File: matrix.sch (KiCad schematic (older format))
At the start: 130 parts, among them SW1 Esc, SW10 9, SW11 0, SW12 -, SW13 =, SW14 Back, SW15 Ins, SW16 Tab, SW17 Q, SW18 W, SW19 E, SW2 1, SW20 R, SW21 T, SW22 Y, SW23 U, SW24 I, SW25 O, SW26 P, SW27 [ {, SW28 ] }, SW29 | \\, SW3 2, SW30 Del, SW31 Caps Lock, SW32 A, SW33 S, SW34 D, SW35 F, SW36 G, SW37 H, SW38 J, SW39 K, SW4 3, SW40 L, SW41 ; :, SW42 ' @, SW43 Enter, SW44 L Shifth, SW45 Z, SW46 X, SW47 C, SW48 V, SW49 B, SW5 4, SW50 N, SW51 M, SW52 , <, SW53 . >, SW54 / ?, SW55 R Shift, SW56 Up, SW57 L Ctrl, SW58 Home, SW59 L Alt, SW6 5, SW60 Space, SW61 R Alt, SW62 Fn, SW63 Left, SW64 Down, SW65 Right, SW7 6, SW8 7, SW9 8

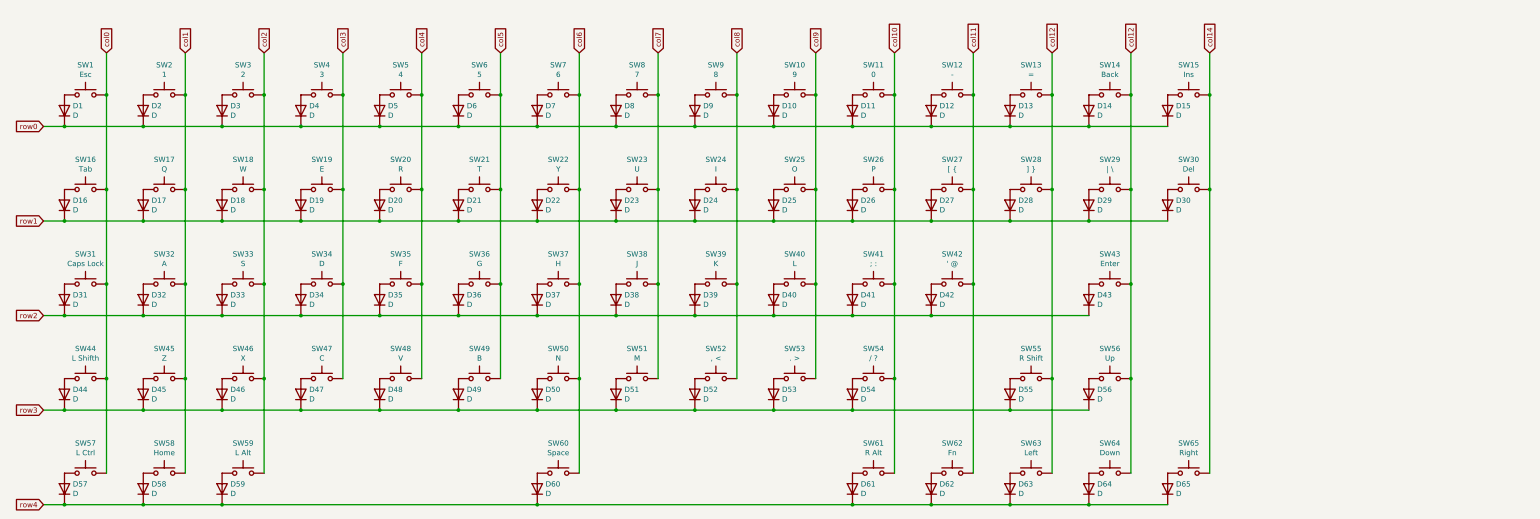
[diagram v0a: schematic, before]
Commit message: change layout and matrix
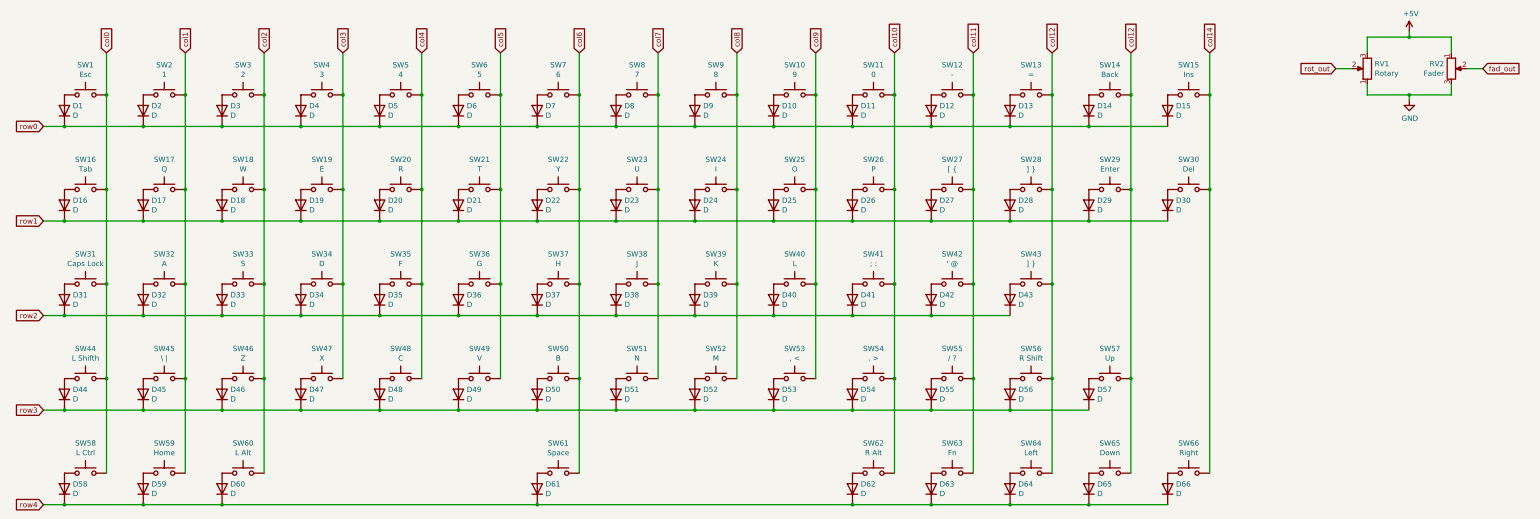
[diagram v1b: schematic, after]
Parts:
- added D55: D, symbol Device:D
- added RV1: Rotary, symbol Device:R_POT
- added RV2: Fader, symbol Device:R_POT
- added SW55: / ?, symbol Switch:SW_Push
- SW29: value | \\ -> Enter
- SW43: value Enter -> ] }
- SW45: value Z -> \\ |
- SW46: value X -> Z
- SW47: value C -> X
- SW48: value V -> C
- SW49: value B -> V
- SW50: value N -> B
- SW51: value M -> N
- SW52: value , < -> M
- SW53: value . > -> , <
- SW54: value / ? -> . >
- renumbered D55 to D56, D56 to D57, D57 to D58, D58 to D59, D59 to D60, D60 to D61, D61 to D62, D62 to D63, D63 to D64, D64 to D65, D65 to D66, SW55 to SW56, SW56 to SW57, SW57 to SW58, SW58 to SW59, SW59 to SW60, SW60 to SW61, SW61 to SW62, SW62 to SW63, SW63 to SW64, SW64 to SW65, SW65 to SW66
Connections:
- net col11: now also SW55.2
- net row3: now also D55.1 (K)
- new net: D55.2 (A), SW55.1
- new net +5V: RV1.3, RV2.1
- new net GND: RV1.1, RV2.3
- new net fad_out: RV2.2
- new net rot_out: RV1.2

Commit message: pcb layout routing WIP
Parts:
- removed D15, D30: D, symbol Device:D
- removed RV1: Rotary, symbol Device:R_POT
- removed SW15: Ins, symbol Switch:SW_Push
- removed SW30: Del, symbol Switch:SW_Push
- added SW66: Rotary, Rotary_Encoder:RotaryEncoder_Alps_EC11E_Vertical_H20mm, symbol Device:Rotary_Encoder
- D1, D10, D11, D12, D13, D14, D2, D3, D4, D5, D6, D7, D8, D9: footprint (none) -> Diode_SMD:D_SOD-123
- D15: renamed from D16; footprint (none) -> Diode_SMD:D_SOD-123
- D16: renamed from D17; footprint (none) -> Diode_SMD:D_SOD-123
- D17: renamed from D18; footprint (none) -> Diode_SMD:D_SOD-123
- D18: renamed from D19; footprint (none) -> Diode_SMD:D_SOD-123
- D19: renamed from D20; footprint (none) -> Diode_SMD:D_SOD-123
- D20: renamed from D21; footprint (none) -> Diode_SMD:D_SOD-123
- D21: renamed from D22; footprint (none) -> Diode_SMD:D_SOD-123
- D22: renamed from D23; footprint (none) -> Diode_SMD:D_SOD-123
- D23: renamed from D24; footprint (none) -> Diode_SMD:D_SOD-123
- D24: renamed from D25; footprint (none) -> Diode_SMD:D_SOD-123
- D25: renamed from D26; footprint (none) -> Diode_SMD:D_SOD-123
- D26: renamed from D27; footprint (none) -> Diode_SMD:D_SOD-123
- D27: renamed from D28; footprint (none) -> Diode_SMD:D_SOD-123
- D28: renamed from D29; footprint (none) -> Diode_SMD:D_SOD-123
- D29: renamed from D31; footprint (none) -> Diode_SMD:D_SOD-123
- D30: renamed from D32; footprint (none) -> Diode_SMD:D_SOD-123
- D31: renamed from D33; footprint (none) -> Diode_SMD:D_SOD-123
- D32: renamed from D34; footprint (none) -> Diode_SMD:D_SOD-123
- D33: renamed from D35; footprint (none) -> Diode_SMD:D_SOD-123
- D34: renamed from D36; footprint (none) -> Diode_SMD:D_SOD-123
- D35: renamed from D37; footprint (none) -> Diode_SMD:D_SOD-123
- D36: renamed from D38; footprint (none) -> Diode_SMD:D_SOD-123
- D37: renamed from D39; footprint (none) -> Diode_SMD:D_SOD-123
- D38: renamed from D40; footprint (none) -> Diode_SMD:D_SOD-123
- D39: renamed from D41; footprint (none) -> Diode_SMD:D_SOD-123
- D40: renamed from D42; footprint (none) -> Diode_SMD:D_SOD-123
- D41: renamed from D43; footprint (none) -> Diode_SMD:D_SOD-123
- D42: renamed from D66; footprint (none) -> Diode_SMD:D_SOD-123
- D43: renamed from D44; footprint (none) -> Diode_SMD:D_SOD-123
- D44: renamed from D45; footprint (none) -> Diode_SMD:D_SOD-123
- D45: renamed from D46; footprint (none) -> Diode_SMD:D_SOD-123
- D46: renamed from D47; footprint (none) -> Diode_SMD:D_SOD-123
- D47: renamed from D48; footprint (none) -> Diode_SMD:D_SOD-123
- D48: renamed from D49; footprint (none) -> Diode_SMD:D_SOD-123
- D49: renamed from D50; footprint (none) -> Diode_SMD:D_SOD-123
- D50: renamed from D51; footprint (none) -> Diode_SMD:D_SOD-123
- D51: renamed from D52; footprint (none) -> Diode_SMD:D_SOD-123
- D52: renamed from D53; footprint (none) -> Diode_SMD:D_SOD-123
- D53: renamed from D54; footprint (none) -> Diode_SMD:D_SOD-123
- D54: renamed from D55; footprint (none) -> Diode_SMD:D_SOD-123
- D55: renamed from D56; footprint (none) -> Diode_SMD:D_SOD-123
- D56: renamed from D57; footprint (none) -> Diode_SMD:D_SOD-123
- D57: renamed from D58; footprint (none) -> Diode_SMD:D_SOD-123
- D58: renamed from D59; footprint (none) -> Diode_SMD:D_SOD-123
- D59: renamed from D60; footprint (none) -> Diode_SMD:D_SOD-123
- D60: renamed from D61; footprint (none) -> Diode_SMD:D_SOD-123
- D61: renamed from D62; footprint (none) -> Diode_SMD:D_SOD-123
- D62: renamed from D63; footprint (none) -> Diode_SMD:D_SOD-123
- D63: renamed from D64; footprint (none) -> Diode_SMD:D_SOD-123
- D64: renamed from D65; footprint (none) -> Diode_SMD:D_SOD-123
- RV2: footprint (none) -> Potentiometer:Potentiometer_Bourns_PTA4543_Single_Slide
- SW1, SW10, SW11, SW12, SW13, SW2, SW3, SW4, SW5, SW6, SW7, SW8, SW9: footprint (none) -> Button_Switch_Keyboard:SW_Cherry_MX_1.00u_PCB
- SW14: footprint (none) -> Button_Switch_Keyboard:SW_Cherry_MX_2.00u_PCB
- SW15: renamed from SW16; footprint (none) -> Button_Switch_Keyboard:SW_Cherry_MX_1.50u_PCB
- SW16: renamed from SW17; footprint (none) -> Button_Switch_Keyboard:SW_Cherry_MX_1.00u_PCB
- SW17: renamed from SW18; footprint (none) -> Button_Switch_Keyboard:SW_Cherry_MX_1.00u_PCB
- SW18: renamed from SW19; footprint (none) -> Button_Switch_Keyboard:SW_Cherry_MX_1.00u_PCB
- SW19: renamed from SW20; footprint (none) -> Button_Switch_Keyboard:SW_Cherry_MX_1.00u_PCB
- SW20: renamed from SW21; footprint (none) -> Button_Switch_Keyboard:SW_Cherry_MX_1.00u_PCB
- SW21: renamed from SW22; footprint (none) -> Button_Switch_Keyboard:SW_Cherry_MX_1.00u_PCB
- SW22: renamed from SW23; footprint (none) -> Button_Switch_Keyboard:SW_Cherry_MX_1.00u_PCB
- SW23: renamed from SW24; footprint (none) -> Button_Switch_Keyboard:SW_Cherry_MX_1.00u_PCB
- SW24: renamed from SW25; footprint (none) -> Button_Switch_Keyboard:SW_Cherry_MX_1.00u_PCB
- SW25: renamed from SW26; footprint (none) -> Button_Switch_Keyboard:SW_Cherry_MX_1.00u_PCB
- SW26: renamed from SW27; footprint (none) -> Button_Switch_Keyboard:SW_Cherry_MX_1.00u_PCB
- SW27: renamed from SW28; footprint (none) -> Button_Switch_Keyboard:SW_Cherry_MX_1.00u_PCB
- SW28: renamed from SW29; footprint (none) -> Button_Switch_Keyboard:SW_Cherry_MX_ISOEnter_PCB
- SW29: renamed from SW31; footprint (none) -> Button_Switch_Keyboard:SW_Cherry_MX_1.75u_PCB
- SW30: renamed from SW32; footprint (none) -> Button_Switch_Keyboard:SW_Cherry_MX_1.00u_PCB
- SW31: renamed from SW33; footprint (none) -> Button_Switch_Keyboard:SW_Cherry_MX_1.00u_PCB
- SW32: renamed from SW34; footprint (none) -> Button_Switch_Keyboard:SW_Cherry_MX_1.00u_PCB
- SW33: renamed from SW35; footprint (none) -> Button_Switch_Keyboard:SW_Cherry_MX_1.00u_PCB
- SW34: renamed from SW36; footprint (none) -> Button_Switch_Keyboard:SW_Cherry_MX_1.00u_PCB
- SW35: renamed from SW37; footprint (none) -> Button_Switch_Keyboard:SW_Cherry_MX_1.00u_PCB
- SW36: renamed from SW38; footprint (none) -> Button_Switch_Keyboard:SW_Cherry_MX_1.00u_PCB
- SW37: renamed from SW39; footprint (none) -> Button_Switch_Keyboard:SW_Cherry_MX_1.00u_PCB
- SW38: renamed from SW40; footprint (none) -> Button_Switch_Keyboard:SW_Cherry_MX_1.00u_PCB
- SW39: renamed from SW41; footprint (none) -> Button_Switch_Keyboard:SW_Cherry_MX_1.00u_PCB
- SW40: renamed from SW42; footprint (none) -> Button_Switch_Keyboard:SW_Cherry_MX_1.00u_PCB
- SW41: renamed from SW43; footprint (none) -> Button_Switch_Keyboard:SW_Cherry_MX_1.00u_PCB
- SW42: renamed from SW66; value Right -> Up; footprint (none) -> Button_Switch_Keyboard:SW_Cherry_MX_1.00u_PCB
- SW43: renamed from SW44; footprint (none) -> Button_Switch_Keyboard:SW_Cherry_MX_1.25u_PCB
- SW44: renamed from SW45; footprint (none) -> Button_Switch_Keyboard:SW_Cherry_MX_1.00u_PCB
- SW45: renamed from SW46; footprint (none) -> Button_Switch_Keyboard:SW_Cherry_MX_1.00u_PCB
- SW46: renamed from SW47; footprint (none) -> Button_Switch_Keyboard:SW_Cherry_MX_1.00u_PCB
- SW47: renamed from SW48; footprint (none) -> Button_Switch_Keyboard:SW_Cherry_MX_1.00u_PCB
- SW48: renamed from SW49; footprint (none) -> Button_Switch_Keyboard:SW_Cherry_MX_1.00u_PCB
- SW49: renamed from SW50; footprint (none) -> Button_Switch_Keyboard:SW_Cherry_MX_1.00u_PCB
- SW50: renamed from SW51; footprint (none) -> Button_Switch_Keyboard:SW_Cherry_MX_1.00u_PCB
- SW51: renamed from SW52; footprint (none) -> Button_Switch_Keyboard:SW_Cherry_MX_1.00u_PCB
- SW52: renamed from SW53; footprint (none) -> Button_Switch_Keyboard:SW_Cherry_MX_1.00u_PCB
- SW53: renamed from SW54; footprint (none) -> Button_Switch_Keyboard:SW_Cherry_MX_1.00u_PCB
- SW54: renamed from SW55; footprint (none) -> Button_Switch_Keyboard:SW_Cherry_MX_1.00u_PCB
- SW55: renamed from SW56; footprint (none) -> Button_Switch_Keyboard:SW_Cherry_MX_1.75u_PCB
- SW56: renamed from SW57; value Up -> Down; footprint (none) -> Button_Switch_Keyboard:SW_Cherry_MX_1.00u_PCB
- SW57: renamed from SW58; footprint (none) -> Button_Switch_Keyboard:SW_Cherry_MX_1.25u_PCB
- SW58: renamed from SW59; footprint (none) -> Button_Switch_Keyboard:SW_Cherry_MX_1.25u_PCB
- SW59: renamed from SW60; footprint (none) -> Button_Switch_Keyboard:SW_Cherry_MX_1.25u_PCB
- SW60: renamed from SW61; footprint (none) -> Button_Switch_Keyboard:SW_Cherry_MX_6.25u_PCB
- SW61: renamed from SW62; footprint (none) -> Button_Switch_Keyboard:SW_Cherry_MX_1.50u_PCB
- SW62: renamed from SW63; footprint (none) -> Button_Switch_Keyboard:SW_Cherry_MX_1.50u_PCB
- SW63: renamed from SW64; footprint (none) -> Button_Switch_Keyboard:SW_Cherry_MX_1.00u_PCB
- SW64: renamed from SW65; value Down -> Right; footprint (none) -> Button_Switch_Keyboard:SW_Cherry_MX_1.00u_PCB
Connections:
- net +5V: now also SW66.B
- net GND: now also SW66.A
- net col12: no longer SW14.2, SW28.2, SW56.2, SW64.2
- net rot_out: now also SW66.C
- net row2: now also D42.1 (K)
- net row4: no longer D42.1 (K)
- net col14 renamed col13
- net col13: now also SW14.2, SW28.2, SW56.2, SW64.2
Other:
- moved on the sheet: D42, SW42

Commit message: add silk screen, Fader65
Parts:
- SW1, SW10, SW11, SW12, SW13, SW16, SW17, SW18, SW19, SW2, SW20, SW21, SW22, SW23, SW24, SW25, SW26, SW27, SW3, SW30, SW31, SW32, SW33, SW34, SW35, SW36, SW37, SW38, SW39, SW4, SW40, SW41, SW42, SW44, SW45, SW46, SW47, SW48, SW49, SW5, SW50, SW51, SW52, SW53, SW54, SW56, SW6, SW63, SW64, SW7, SW8, SW9: footprint Button_Switch_Keyboard:SW_Cherry_MX_1.00u_PCB -> mx_suruq:SW_Cherry_MX_1.00u_PCB_NameSilk
- SW14: footprint Button_Switch_Keyboard:SW_Cherry_MX_2.00u_PCB -> mx_suruq:SW_Cherry_MX_2.00u_PCB_NameSilk
- SW15, SW61, SW62: footprint Button_Switch_Keyboard:SW_Cherry_MX_1.50u_PCB -> mx_suruq:SW_Cherry_MX_1.50u_PCB_NameSilk
- SW28: footprint Button_Switch_Keyboard:SW_Cherry_MX_ISOEnter_PCB -> mx_suruq:SW_Cherry_MX_ISOEnter_PCB_NameSilk
- SW29, SW55: footprint Button_Switch_Keyboard:SW_Cherry_MX_1.75u_PCB -> mx_suruq:SW_Cherry_MX_1.75u_PCB_NameSilk
- SW43, SW57, SW58, SW59: footprint Button_Switch_Keyboard:SW_Cherry_MX_1.25u_PCB -> mx_suruq:SW_Cherry_MX_1.25u_PCB_NameSilk
- SW60: footprint Button_Switch_Keyboard:SW_Cherry_MX_6.25u_PCB -> mx_suruq:SW_Cherry_MX_6.25u_PCB_NameSilk
